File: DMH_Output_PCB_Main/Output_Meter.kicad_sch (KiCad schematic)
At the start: 63 parts, among them Q1 BC558, Q2 BC558, U1 TL072, U2 LM339, U3 LM339, U4 LM339, U5 LM339, U6 LM339

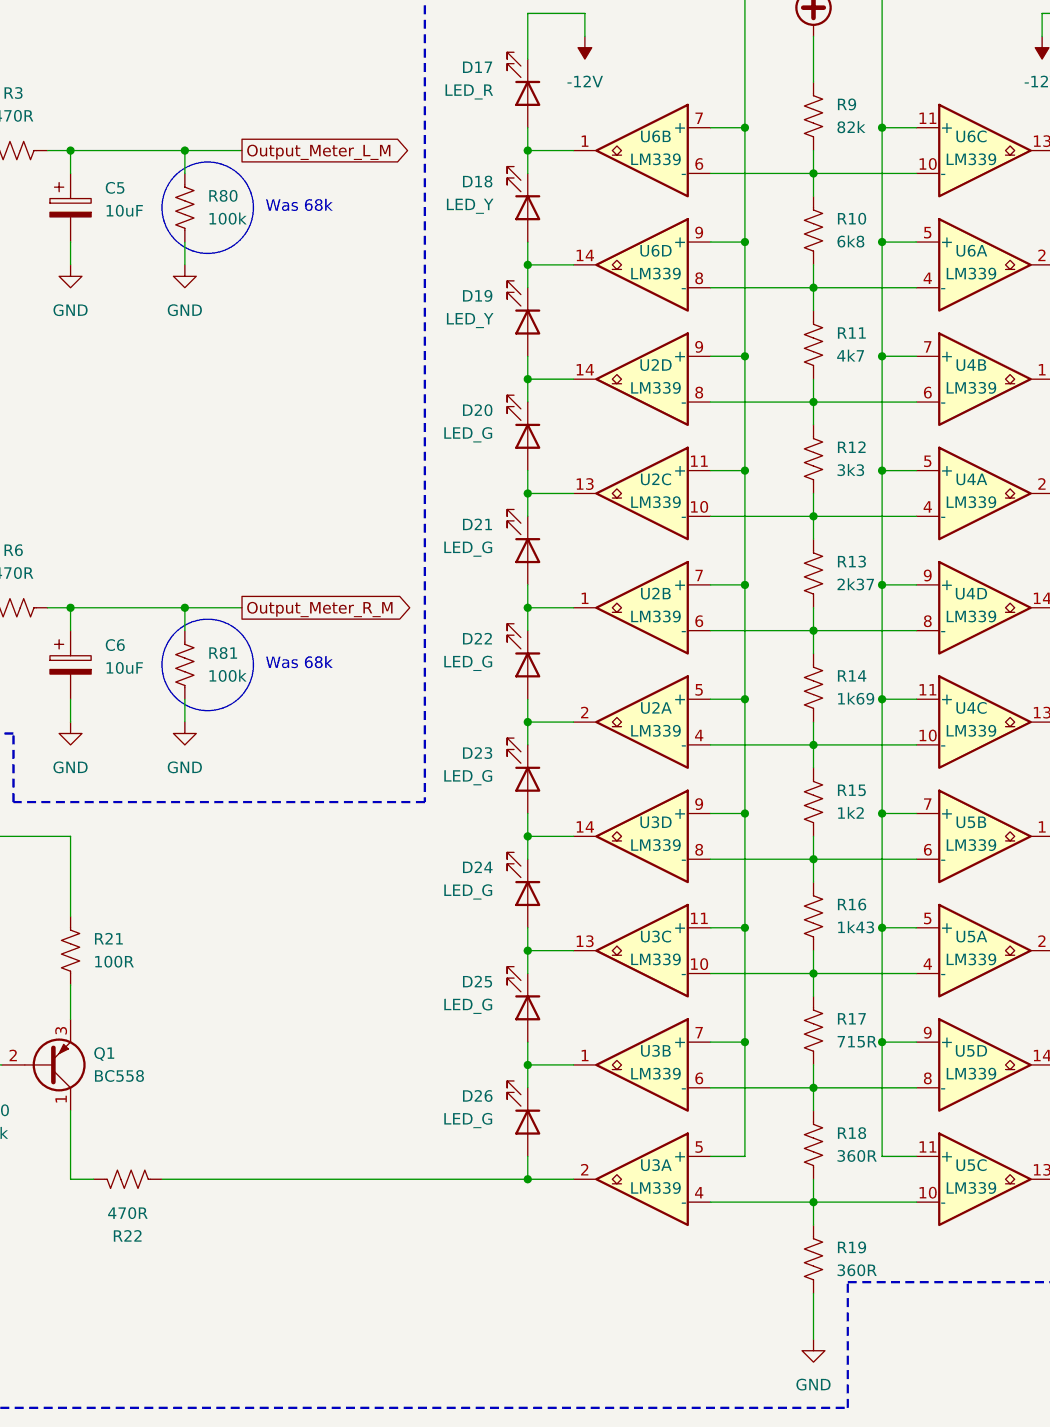
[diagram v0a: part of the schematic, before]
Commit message: Adjustments during prototyping
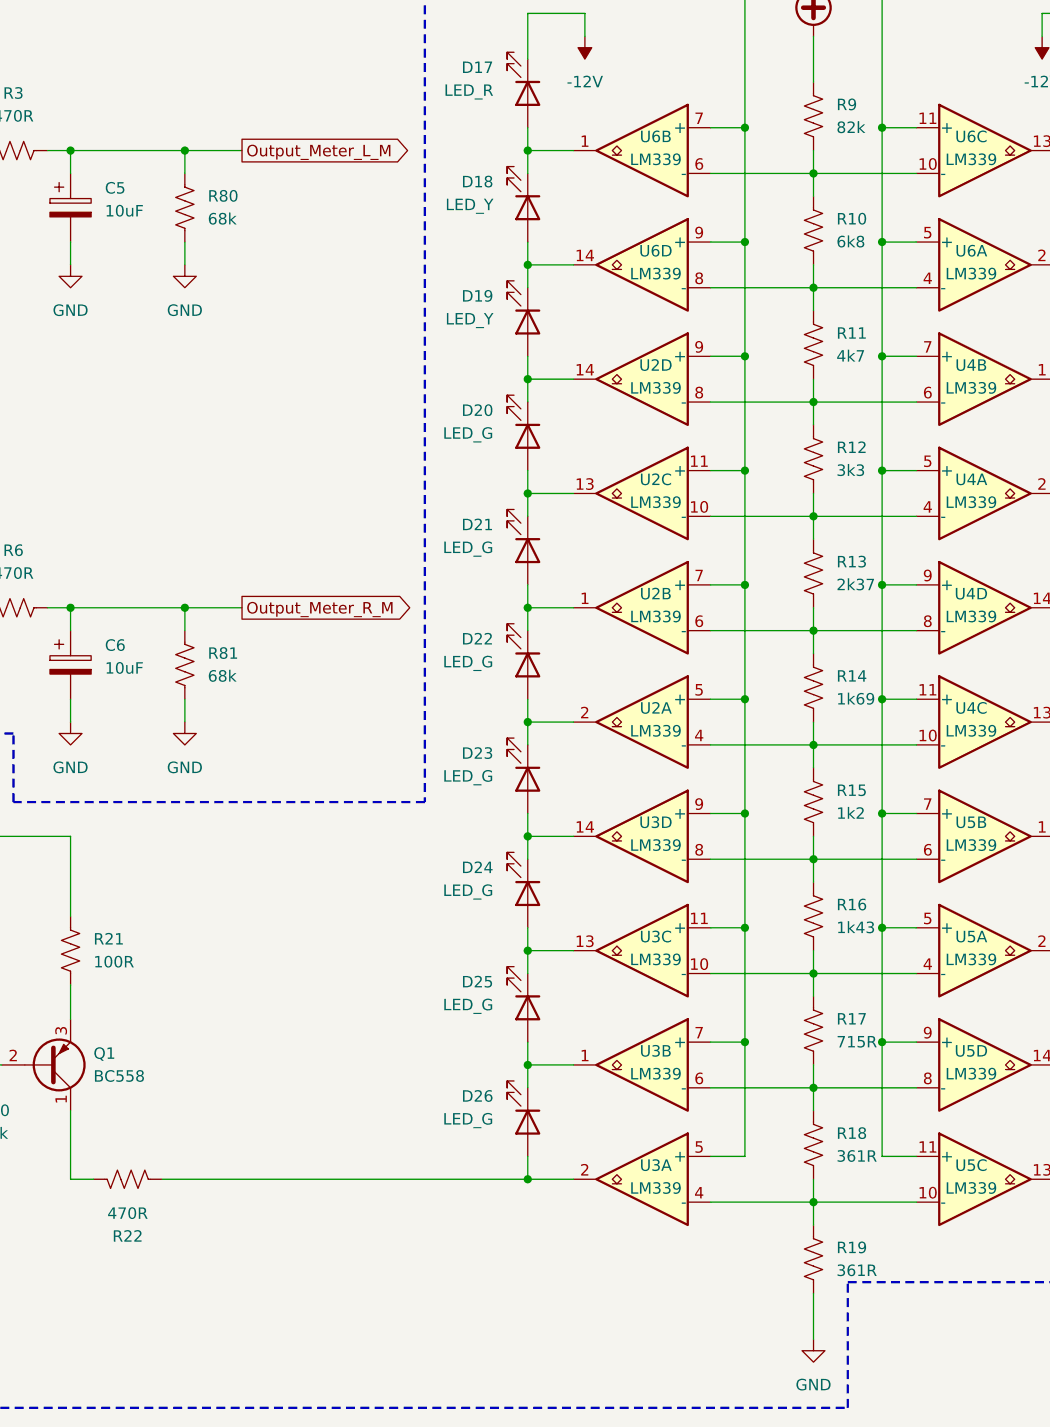
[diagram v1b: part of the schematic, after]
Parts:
- R18, R19: value 360R -> 361R
- R80, R81: value 100k -> 68k
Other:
- note removed: "Was 68k"
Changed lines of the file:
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@@
 		(comment 1 "PCB for 5 cm Kosmo format synthesizer module")
 	)
-	(circle
-		(center 104.14 95.25)
-		(radius 5.08)
-		(stroke
-			(width 0)
-			(type default)
-		)
-		(fill
-			(type none)
-		)
-	)
-	(circle
-		(center 104.14 44.45)
-		(radius 5.08)
-		(stroke
-			(width 0)
-			(type default)
-		)
-		(fill
-			(type none)
-		)
-	)
-	(text "Was 68k"
-		(exclude_from_sim no)
-		(at 114.3 44.45 0)
-		(effects
-			(font
-				(size 1.27 1.27)
-			)
-		)
-	)
 	(text "Controls PCB"
 		(exclude_from_sim no)
@@
 		)
 	)
-	(text "Was 68k"
-		(exclude_from_sim no)
-		(at 114.3 95.25 0)
-		(effects
-			(font
-				(size 1.27 1.27)
-			)
-		)
-	)
 	(junction
 		(at 139.7 139.7)
@@
 			)
 		)
-		(property "Value" "100k"
+		(property "Value" "68k"
 			(at 104.14 45.7199 0)
 			(effects
@@
 			)
 		)
-		(property "Value" "360R"
+		(property "Value" "361R"
 			(at 173.99 149.8599 0)
 			(effects
@@
 			)
 		)
-		(property "Value" "100k"
+		(property "Value" "68k"
 			(at 104.14 96.5199 0)
 			(effects
@@
 			)
 		)
-		(property "Value" "360R"
+		(property "Value" "361R"
 			(at 173.99 162.5599 0)
 			(effects

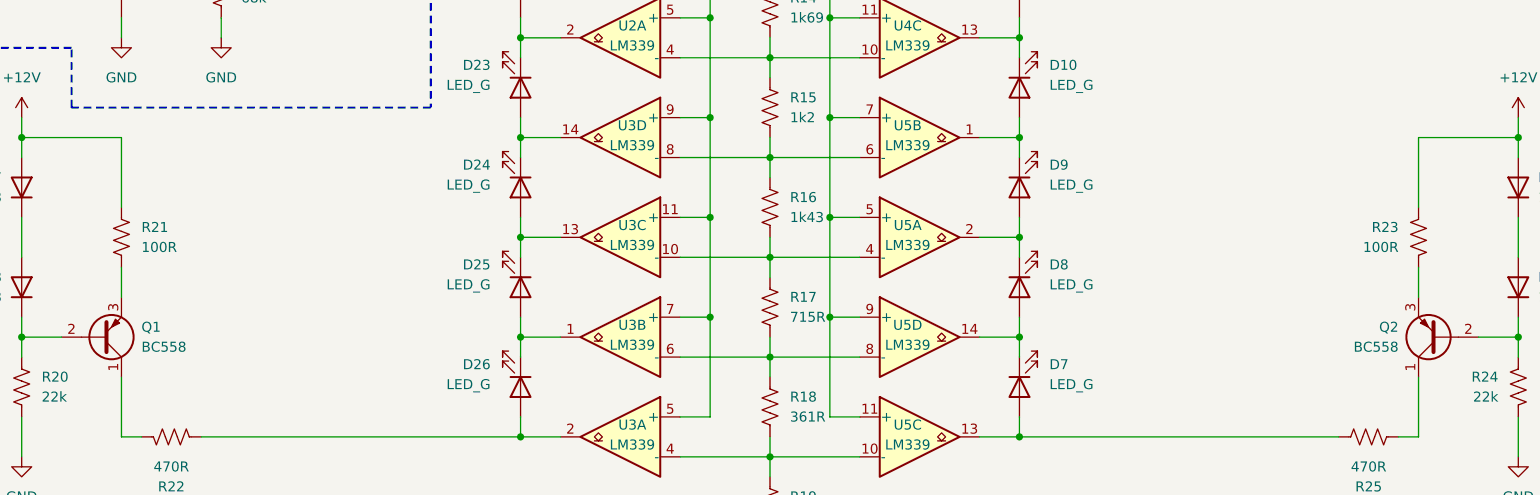
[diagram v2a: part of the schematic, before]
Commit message: Replaced jack symbols with 5pin ones
Also updated Meter LED current source resistor to 75R
Also increased LED guiding PCB mounting holes to M2.5
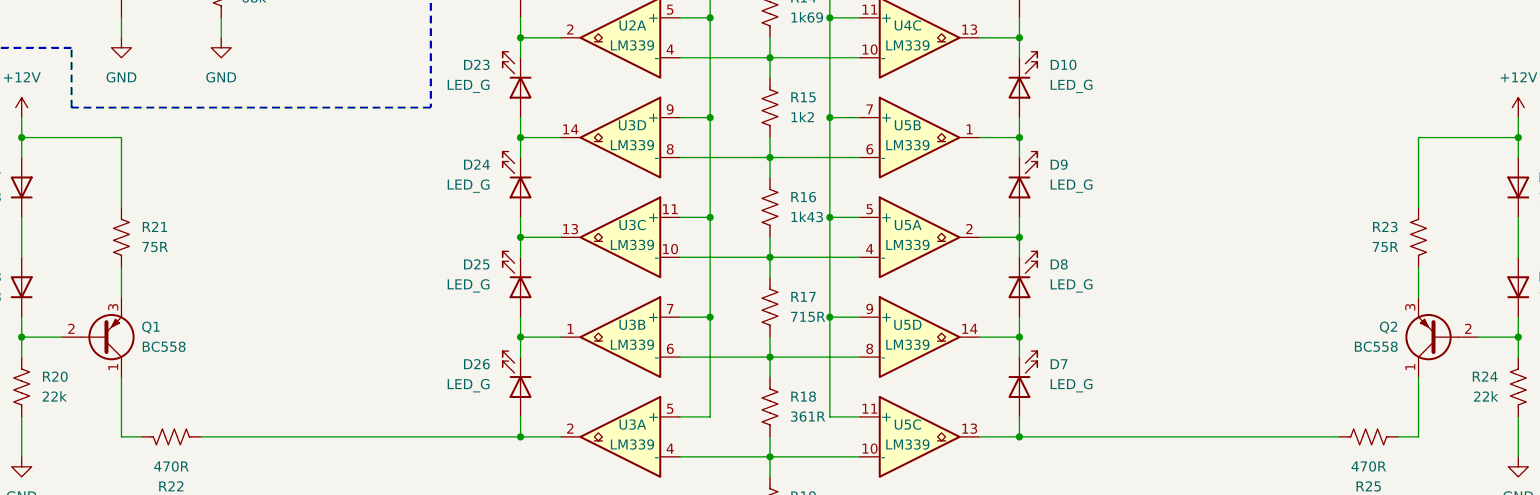
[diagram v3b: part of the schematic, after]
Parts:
- R21, R23: value 100R -> 75R
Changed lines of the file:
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@@
 			)
 		)
-		(property "Value" "100R"
+		(property "Value" "75R"
 			(at 251.46 128.2699 0)
 			(show_name no)
@@
 			)
 		)
-		(property "Value" "100R"
+		(property "Value" "75R"
 			(at 91.44 128.2699 0)
 			(show_name no)

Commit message: Prepped for Main PCB design
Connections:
- net Meter_Left renamed L_Out_Meter_M
- net Meter_Right renamed R_Out_Meter_M
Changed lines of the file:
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@@
 		)
 	)
-	(hierarchical_label "Meter_Left"
+	(hierarchical_label "L_Out_Meter_M"
 		(shape input)
 		(at 25.4 48.26 180)
@@
 		)
 	)
-	(hierarchical_label "Meter_Right"
+	(hierarchical_label "R_Out_Meter_M"
 		(shape input)
 		(at 25.4 99.06 180)
